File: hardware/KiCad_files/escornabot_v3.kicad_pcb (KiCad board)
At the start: 2 copper layers, 55 x 110.1 mm, 131 parts, among them IC1 ULN2803, U1 CONN_01X04, U2 ESP01, U3 CONN_01X04, U4 CONN_01X04, U5 CONN_01X04, U6 LM1117-SOT, X1 Screw_Terminal_1x02

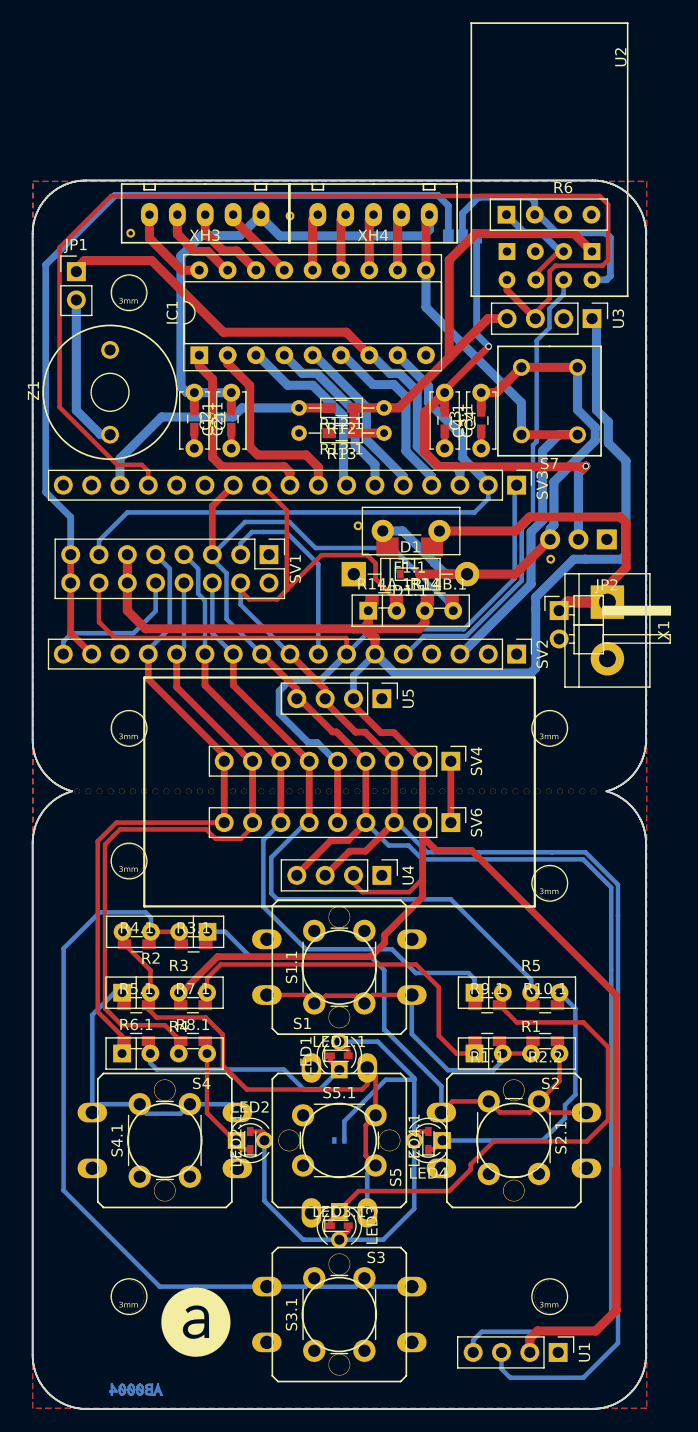
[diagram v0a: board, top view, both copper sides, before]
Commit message: Actualización del fichero de layout con las cotas de los drills para la fijacion
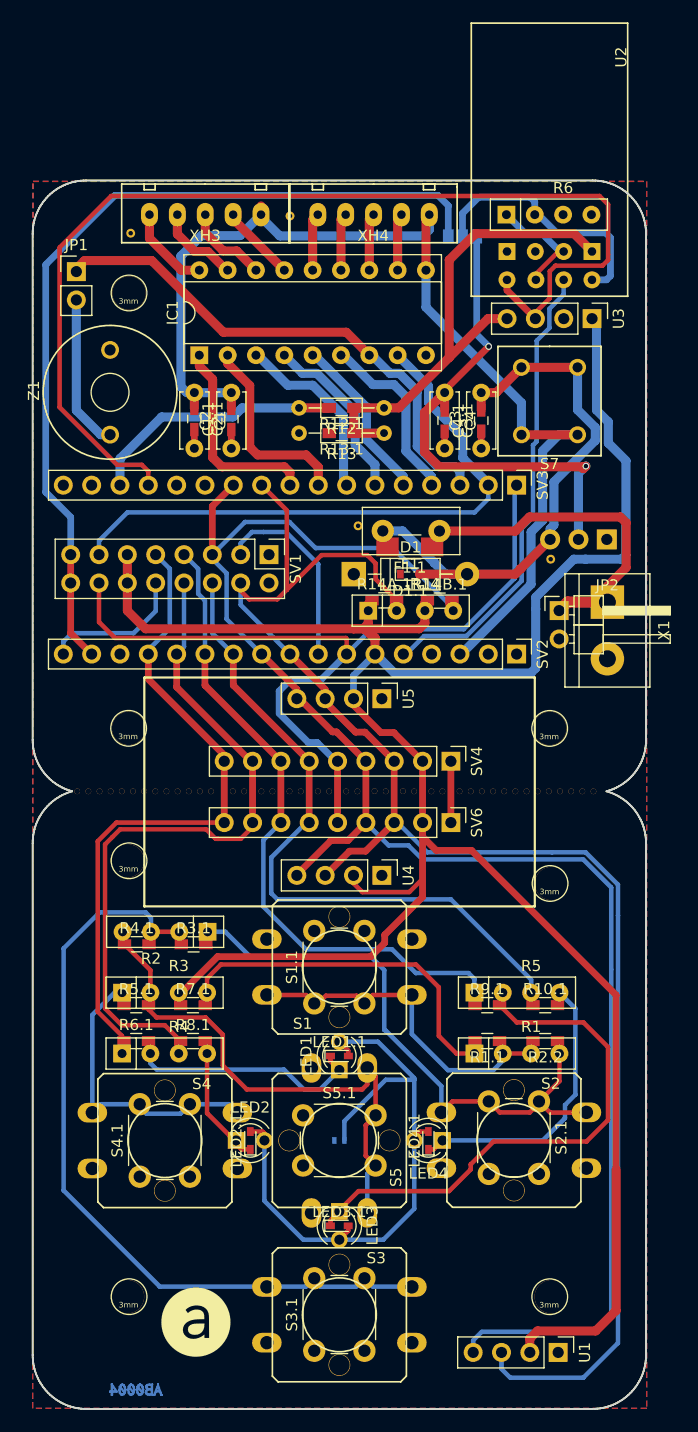
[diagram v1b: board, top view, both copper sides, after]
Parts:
- ?: value (none) -> G***
- svg2mod: renamed from edge; value (none) -> G***
